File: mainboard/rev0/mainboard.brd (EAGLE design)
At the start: 100 x 80 mm, 11 parts

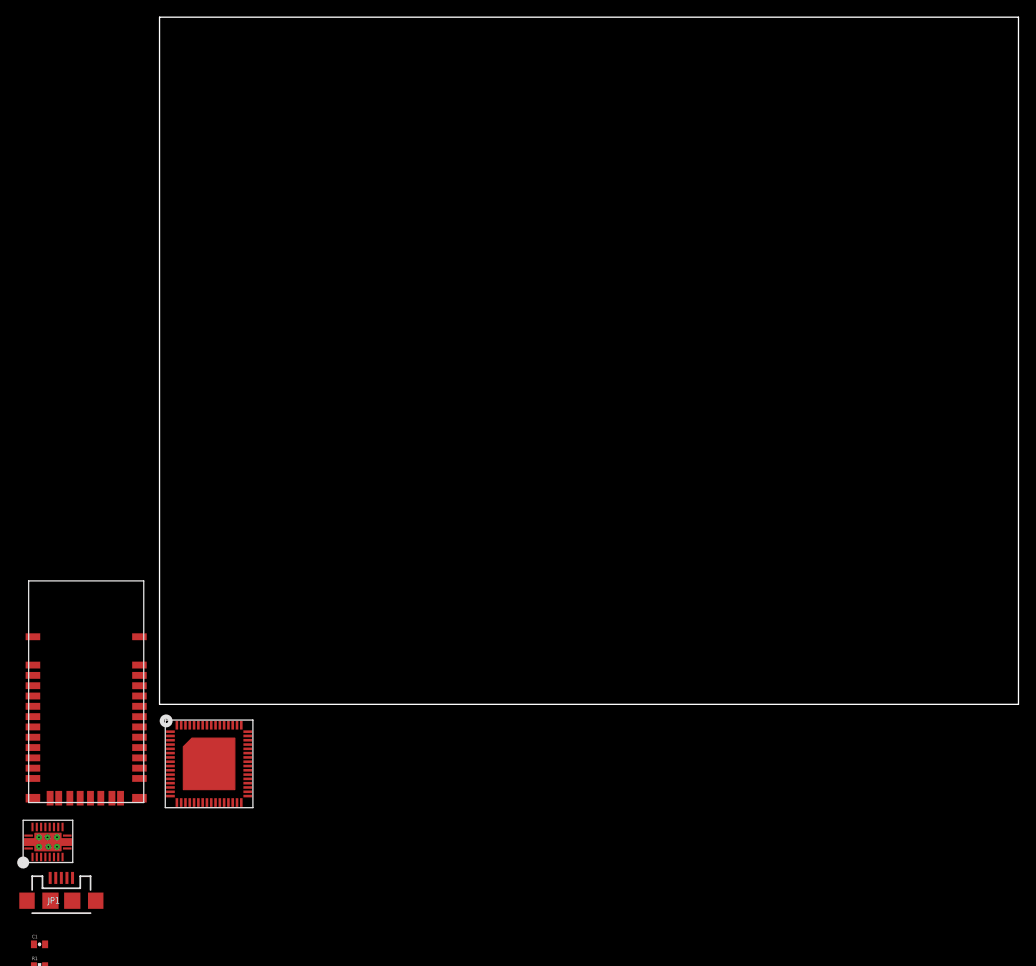
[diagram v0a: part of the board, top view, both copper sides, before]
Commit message: cleaned up schematic
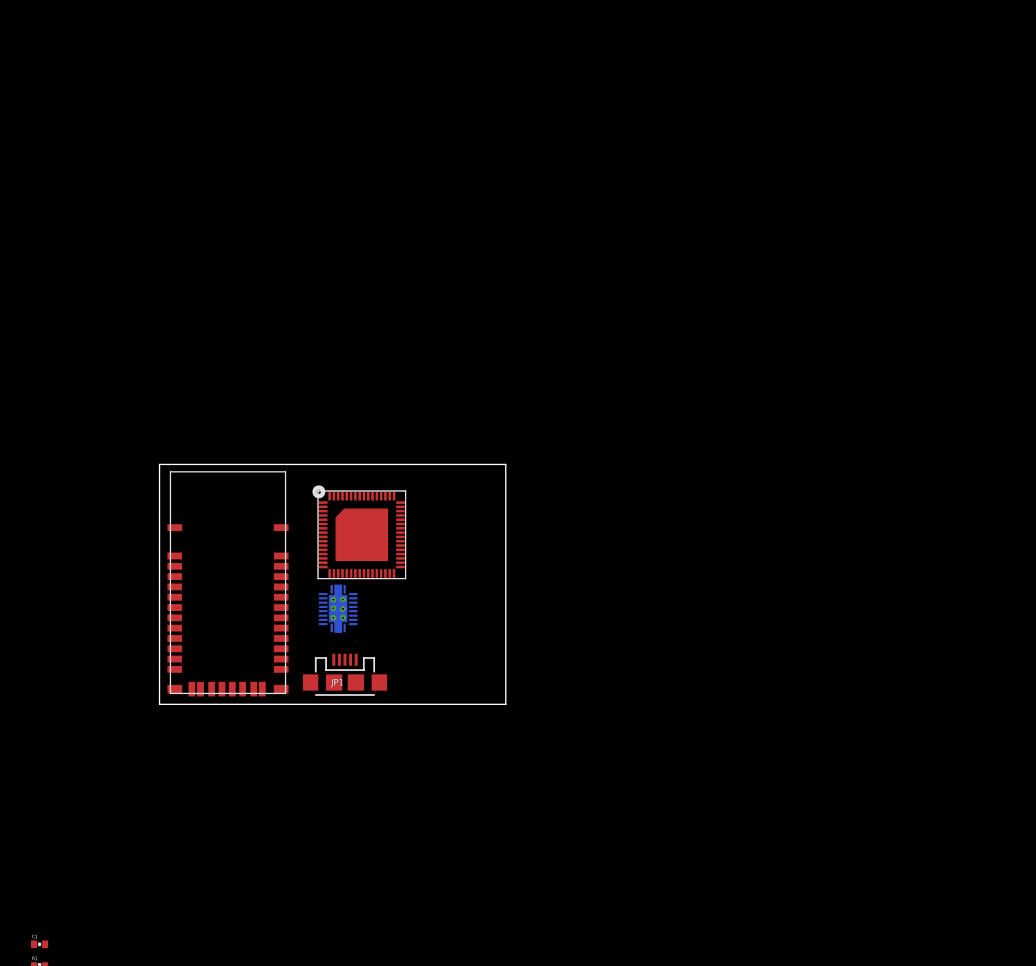
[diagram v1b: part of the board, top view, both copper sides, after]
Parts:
- moved U$3 43.4 mm to (19.1, 8.89), flipped to the bottom, turned to 90 degrees
- moved JP1 41.7 mm to (21.6, 2.54)
- moved U$1 32.1 mm to (19.1, 15.2)
- moved U$2 20.8 mm to (1.27, 1.27)
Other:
- board size 100 x 80 mm -> 40.3 x 27.9 mm
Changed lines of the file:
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@@
 <setting verticaltext="up"/>
 </settings>
-<grid distance="0.05" unitdist="inch" unit="inch" style="lines" multiple="1" display="no" altdistance="0.025" altunitdist="inch" altunit="inch"/>
+<grid distance="100" unitdist="mil" unit="mil" style="lines" multiple="1" display="no" altdistance="50" altunitdist="mil" altunit="mil"/>
 <layers>
 <layer number="1" name="Top" color="4" fill="1" visible="yes" active="yes"/>
@@
 <board>
 <plain>
-<wire x1="0" y1="0" x2="100" y2="0" width="0" layer="20"/>
-<wire x1="100" y1="0" x2="100" y2="80" width="0" layer="20"/>
-<wire x1="100" y1="80" x2="0" y2="80" width="0" layer="20"/>
-<wire x1="0" y1="80" x2="0" y2="0" width="0" layer="20"/>
+<wire x1="0" y1="0" x2="40.31" y2="0" width="0" layer="20"/>
+<wire x1="40.31" y1="0" x2="40.31" y2="27.93" width="0" layer="20"/>
+<wire x1="40.31" y1="27.93" x2="0" y2="27.93" width="0" layer="20"/>
+<wire x1="0" y1="27.93" x2="0" y2="0" width="0" layer="20"/>
+<dimension x1="45.39" y1="27.93" x2="0" y2="27.93" x3="22.695" y3="35.56" textsize="1.778" layer="20" unit="mil"/>
+<dimension x1="45.39" y1="0" x2="45.39" y2="27.93" x3="53.34" y3="13.965" textsize="1.778" layer="20" unit="mil"/>
 </plain>
 <attributes>
@@
 </autorouter>
 <elements>
-<element name="U$1" library="TuansLib" package="VQFN_RGC_64PIN" value="MSP430F5528" x="1.27" y="-11.43"/>
-<element name="U$2" library="TuansLib" package="RN-42" value="RN-42" x="-15.24" y="-11.43"/>
-<element name="U$3" library="TuansLib" package="VQFN_RHL_20PIN" value="BQ25010" x="-15.24" y="-17.78"/>
-<element name="JP1" library="SparkFun-Connectors" package="USB-MICROB" value="USB-MICROB" x="-11.43" y="-22.86">
-<attribute name="PROD_ID" value="CONN-09505" x="-11.43" y="-22.86" size="1.778" layer="27" display="off"/>
+<element name="U$1" library="TuansLib" package="VQFN_RGC_64PIN" value="MSP430F5528" x="19.05" y="15.24"/>
+<element name="U$2" library="TuansLib" package="RN-42" value="RN-42" x="1.27" y="1.27"/>
+<element name="U$3" library="TuansLib" package="VQFN_RHL_20PIN" value="BQ25010" x="19.05" y="8.89" rot="MR90"/>
+<element name="JP1" library="SparkFun-Connectors" package="USB-MICROB" value="USB-MICROB" x="21.59" y="2.54">
+<attribute name="PROD_ID" value="CONN-09505" x="21.59" y="2.54" size="1.778" layer="27" display="off"/>
 </element>
 <element name="C1" library="SparkFun-Capacitors" package="0402-CAP" value="" x="-13.97" y="-27.94"/>
@@
 <contactref element="JP1" pad="GND"/>
 <contactref element="C1" pad="2"/>
-<wire x1="-15.43" y1="-22.86" x2="-13.32" y2="-27.94" width="0" layer="19" extent="1-1"/>
-<wire x1="-14.29" y1="-17.78" x2="-15.43" y2="-22.86" width="0" layer="19" extent="1-1"/>
-<wire x1="-11.29" y1="-17.78" x2="-14.29" y2="-17.78" width="0" layer="19" extent="1-1"/>
-<wire x1="-10.13" y1="-20.21" x2="-11.29" y2="-17.78" width="0" layer="19" extent="1-1"/>
-<wire x1="-14.29" y1="-14.28" x2="-14.29" y2="-17.78" width="0" layer="19" extent="1-1"/>
-<wire x1="-7.43" y1="-22.86" x2="-10.13" y2="-20.21" width="0" layer="19" extent="1-1"/>
-<wire x1="-11.74" y1="-10.93" x2="-14.29" y2="-14.28" width="0" layer="19" extent="1-1"/>
-<wire x1="-14.74" y1="-8.63" x2="-11.74" y2="-10.93" width="0" layer="19" extent="1-1"/>
-<wire x1="-5.54" y1="-10.93" x2="-11.74" y2="-10.93" width="0" layer="19" extent="1-1"/>
-<wire x1="1.27" y1="-10.68" x2="-5.54" y2="-10.93" width="0" layer="19" extent="1-1"/>
-<wire x1="1.27" y1="-9.68" x2="1.27" y2="-10.68" width="0" layer="19" extent="1-1"/>
-<wire x1="6.02" y1="-2.43" x2="1.27" y2="-9.68" width="0" layer="19" extent="1-1"/>
-<wire x1="9.52" y1="-2.43" x2="6.02" y2="-2.43" width="0" layer="19" extent="1-1"/>
-<wire x1="10.27" y1="-7.68" x2="9.52" y2="-2.43" width="0" layer="19" extent="1-1"/>
-<wire x1="-14.74" y1="4.57" x2="-14.74" y2="-8.63" width="0" layer="19" extent="1-1"/>
+<wire x1="17.59" y1="2.54" x2="-13.32" y2="-27.94" width="0" layer="19" extent="1-1"/>
+<wire x1="19.05" y1="9.84" x2="17.59" y2="2.54" width="0" layer="19" extent="1-1"/>
+<wire x1="19.05" y1="12.84" x2="19.05" y2="9.84" width="0" layer="19" extent="1-1"/>
+<wire x1="22.89" y1="5.19" x2="19.05" y2="12.84" width="0" layer="19" extent="1-1"/>
+<wire x1="22.55" y1="9.84" x2="19.05" y2="9.84" width="0" layer="19" extent="1-1"/>
+<wire x1="25.59" y1="2.54" x2="22.89" y2="5.19" width="0" layer="19" extent="1-1"/>
+<wire x1="4.77" y1="1.77" x2="22.55" y2="9.84" width="0" layer="19" extent="1-1"/>
+<wire x1="1.77" y1="4.07" x2="4.77" y2="1.77" width="0" layer="19" extent="1-1"/>
+<wire x1="10.97" y1="1.77" x2="4.77" y2="1.77" width="0" layer="19" extent="1-1"/>
+<wire x1="19.05" y1="15.99" x2="10.97" y2="1.77" width="0" layer="19" extent="1-1"/>
+<wire x1="19.05" y1="16.99" x2="19.05" y2="15.99" width="0" layer="19" extent="1-1"/>
+<wire x1="23.8" y1="24.24" x2="19.05" y2="16.99" width="0" layer="19" extent="1-1"/>
+<wire x1="27.3" y1="24.24" x2="23.8" y2="24.24" width="0" layer="19" extent="1-1"/>
+<wire x1="28.05" y1="18.99" x2="27.3" y2="24.24" width="0" layer="19" extent="1-1"/>
+<wire x1="1.77" y1="17.27" x2="1.77" y2="4.07" width="0" layer="19" extent="1-1"/>
 </signal>
 <signal name="N$1">
 <contactref element="JP1" pad="VBUS"/>
 <contactref element="C1" pad="1"/>
-<wire x1="-12.73" y1="-20.21" x2="-14.62" y2="-27.94" width="0" layer="19" extent="1-1"/>
+<wire x1="20.29" y1="5.19" x2="-14.62" y2="-27.94" width="0" layer="19" extent="1-1"/>
 </signal>
 </signals>

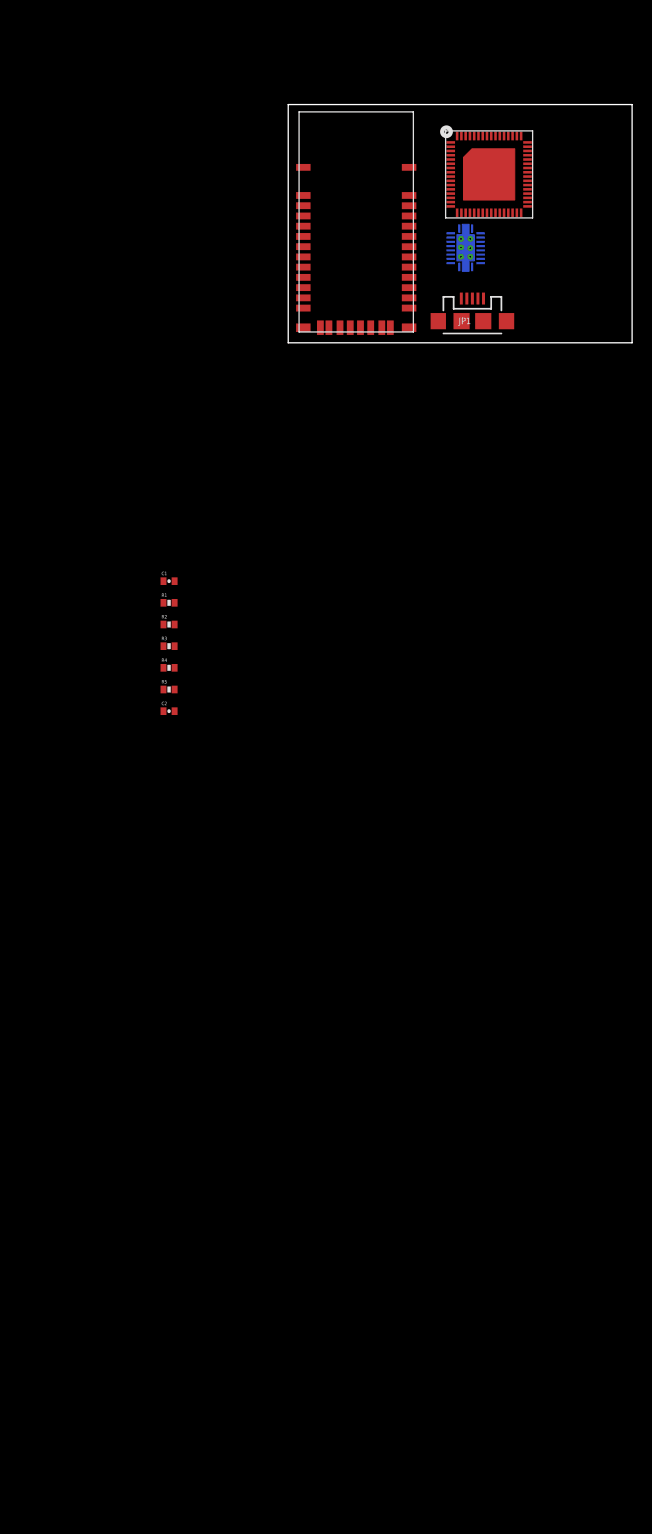
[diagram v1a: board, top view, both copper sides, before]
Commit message: added the buttons garrett wanted
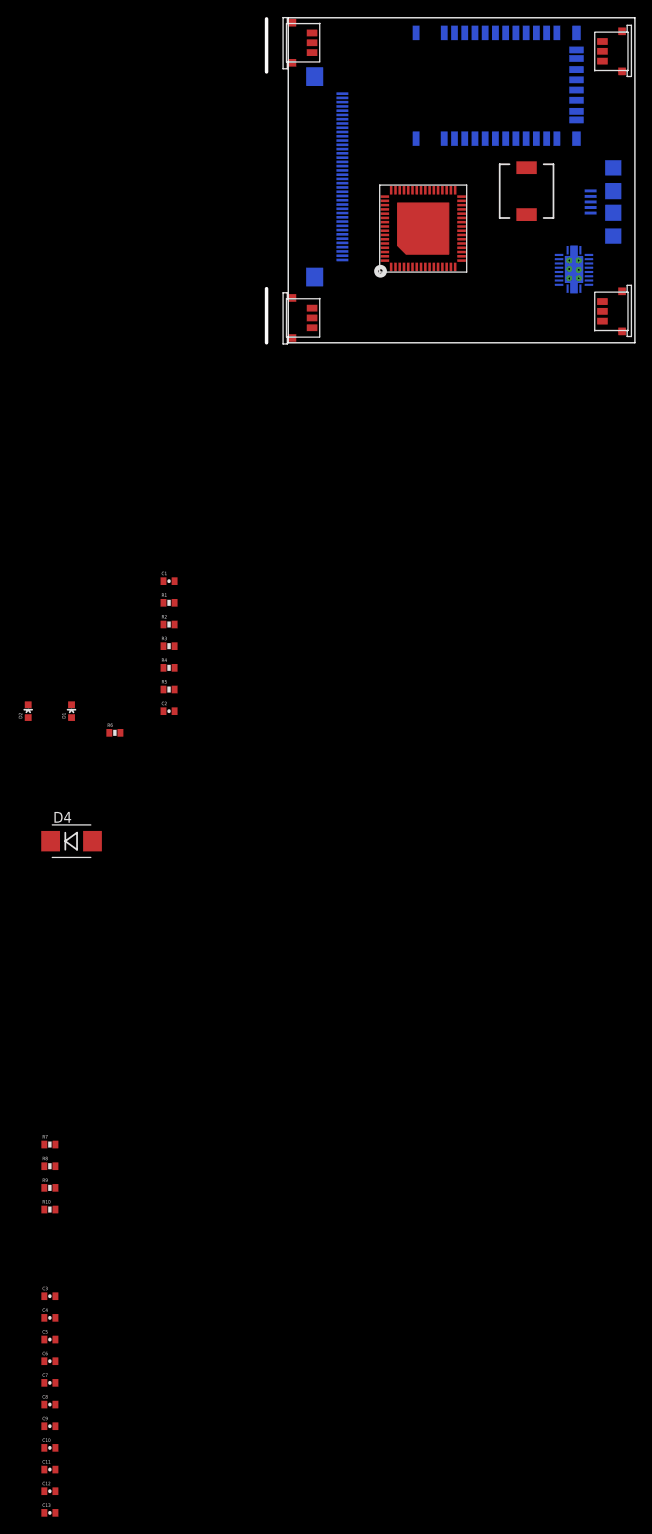
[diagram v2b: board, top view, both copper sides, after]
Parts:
- added C10, C11, C12, C13, C3, C4, C5, C6, C7, C8, C9: (no value), SparkFun-Capacitors:0402-CAP
- added D1, D2: BLUE, SparkFun-LED:LED-0603
- added D4: (no value), SparkFun-DiscreteSemi:DIODE-HV
- added L1: (no value), SparkFun-Passives:B82462G
- added R10, R6, R7, R8, R9: (no value), SparkFun-Passives:0402-RES
- added U$4, U$5, U$6, U$7: EVP-AEDB2A, TuansLib:EVP-AEDB2A
- added U$8: FH12-40S-0.5SH, TuansLib:FH12-40S-0.5SH
- moved U$2 48.5 mm to (34.3, 36.8), flipped to the bottom, turned to 270 degrees
- moved JP1 21.6 mm to (38.1, 16.5), flipped to the bottom, turned to 270 degrees
- moved U$3 13.0 mm to (31.8, 6.35)
- moved U$1 6.48 mm to (20.3, 8.89), turned to 90 degrees
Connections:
- new net BATT_PWR: R6.2, U$3.16, U$3.17
- new net BT_BAUD: U$1.48, U$2.4
- new net BT_CONN: U$1.47, U$2.19
- new net N$10: R4.1, U$3.7
- new net N$11: R3.1, U$3.8
- new net N$12: R6.1, U$3.4
- new net N$13: R7.2, U$4.1, U$4.1'
- new net N$14: R8.2, U$5.1, U$5.1'
- new net N$15: R9.2, U$6.1, U$6.1'
- new net N$16: R10.2, U$7.1, U$7.1'
- new net N$17: R7.1
- new net N$18: R8.1
- new net N$19: R9.1
- new net N$2: D1.C, R4.2
- new net N$20: R10.1
- new net N$21: U$8.4
- new net N$22: U$8.5
- new net N$23: U$8.6
- new net N$24: U$8.7
- new net N$25: U$8.8
- new net N$26: C4.2, U$8.10
- new net N$27: C4.1, U$8.11
- new net N$28: C5.2, U$8.12
- new net N$29: C5.1, U$8.13
- new net N$3: D4.C, U$3.13
- new net N$30: C6.2, U$8.14
- new net N$31: C6.1, U$8.15
- new net N$32: C7.2, U$8.16
- new net N$33: C7.1, U$8.17
- new net N$34: C8.2, U$8.18
- new net N$35: C8.1, U$8.19
- new net N$36: C9.1, U$8.20
- new net N$37: C9.2, U$8.21
- new net N$38: C10.1, U$8.22
- new net N$39: C10.2, U$8.23
- new net N$4: D2.C, R3.2
- new net N$40: C11.1, U$8.24
- new net N$41: C11.2, U$8.25
- new net N$42: C12.1, U$8.26
- new net N$43: C12.2, U$8.27
- new net N$44: C13.1, U$8.28
- new net N$45: C13.2, U$8.29
- new net N$46: C3.2, U$8.9
- new net N$5: R1.1, R2.2, U$3.2
- new net N$6: L1.P$1, U$3.19
- new net N$7: U$8.1
- new net N$8: U$8.2
- new net SPI_CLK: U$1.44
- new net SPI_MISO: U$1.43
- new net SPI_MOSI: U$1.42
- new net SPI_STE: U$1.41
- new net UART_RX: U$1.46, U$2.14
- new net UART_TX: U$1.45, U$2.13
- new net VCC: C2.1, L1.P$2, R1.2, U$2.11
- new net VUSB: C1.1, D1.A, D2.A, D4.A, JP1.VBUS, U$3.6
- net GND: now also C2.2, C3.1, R2.1, R5.2, U$3.15, U$3.20, U$4.2, U$5.2, U$6.2, U$7.2, U$8.3
- net N$1: now also R5.1, U$3.12; no longer C1.1, JP1.VBUS
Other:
- board size 40.3 x 27.9 mm -> 43.2 x 38.1 mm

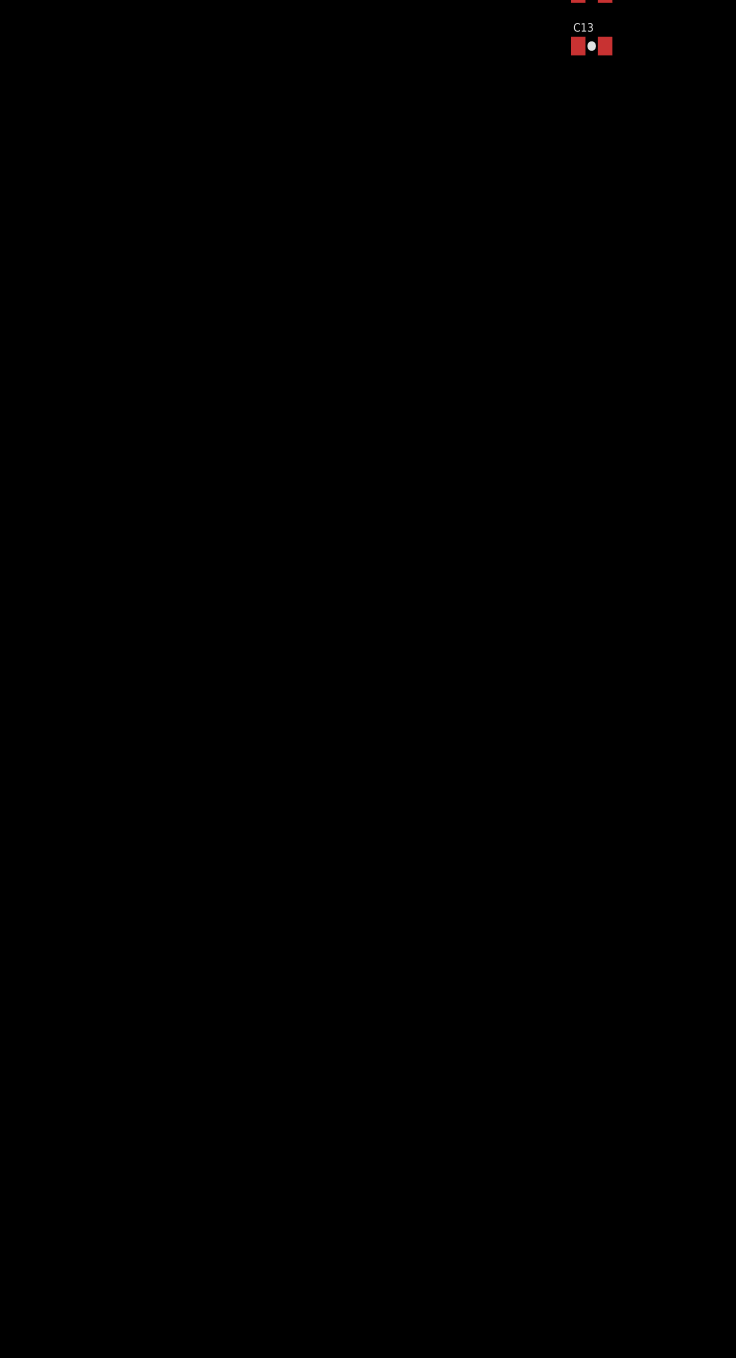
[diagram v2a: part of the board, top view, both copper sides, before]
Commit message: Completed EPD connector schematic needs to be reviewed before sent out
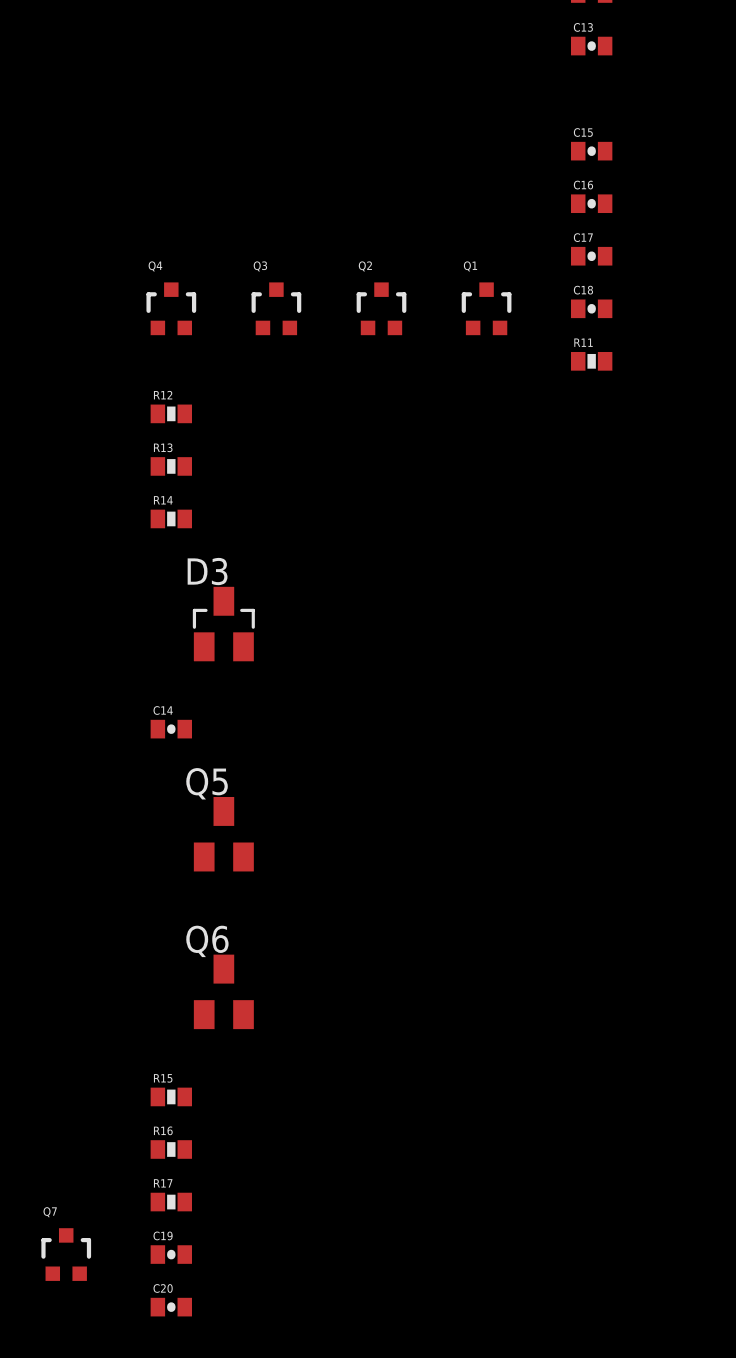
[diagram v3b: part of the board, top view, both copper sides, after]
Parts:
- added C14, C15, C16, C17, C18, C19, C20: (no value), SparkFun-Capacitors:0402-CAP
- added D3: BAT54S, diode:SOT23
- added Q1, Q2, Q3, Q4, Q7: MOSFET-NCHANNEL2N7002PW, SparkFun-DiscreteSemi:SOT323
- added Q5, Q6: BSS84, transistor-small-signal:SOT23
- added R11, R12, R13, R14, R15, R16, R17: (no value), SparkFun-Passives:0402-RES
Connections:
- new net BORDER: Q3.3, R14.1, U$8.38
- new net EPD_BORDER: Q4.1
- new net EPD_DISCHARGE: Q1.1, Q2.1
- new net EPD_PANEL: Q5.1, Q7.1
- new net EPD_PWM: C14.1
- new net N$47: Q6.3, R15.1, R16.2
- new net N$49: Q3.1, R12.1, R13.1
- new net N$50: C20.2, Q5.3, Q6.1, R17.1
- new net N$52: Q7.3, R17.2
- new net N$53: Q4.3, R13.2
- new net N$9: C14.2, D3.3
- new net VCC_T: C19.2, Q4.2, R15.2, U$8.31, U$8.32
- new net VCOM: R11.2, R14.2, U$8.39, U$8.40
- new net VCOM_DRIVER: U$8.30
- new net VDH: C17.2, Q1.3, U$8.36
- new net VDL: C18.2, Q3.2, R12.2, U$8.37
- new net VGH: C15.2, Q2.3, U$8.34
- new net VGL: C16.2, D3.1, U$8.35
- net GND: now also C15.1, C16.1, C17.1, C18.1, C19.1, C20.1, D3.2, Q1.2, Q2.2, Q7.2, R16.1, U$8.33
- net VCC: now also Q5.2, Q6.2
